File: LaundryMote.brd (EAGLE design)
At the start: 52.5 x 23.3 mm, 6 parts

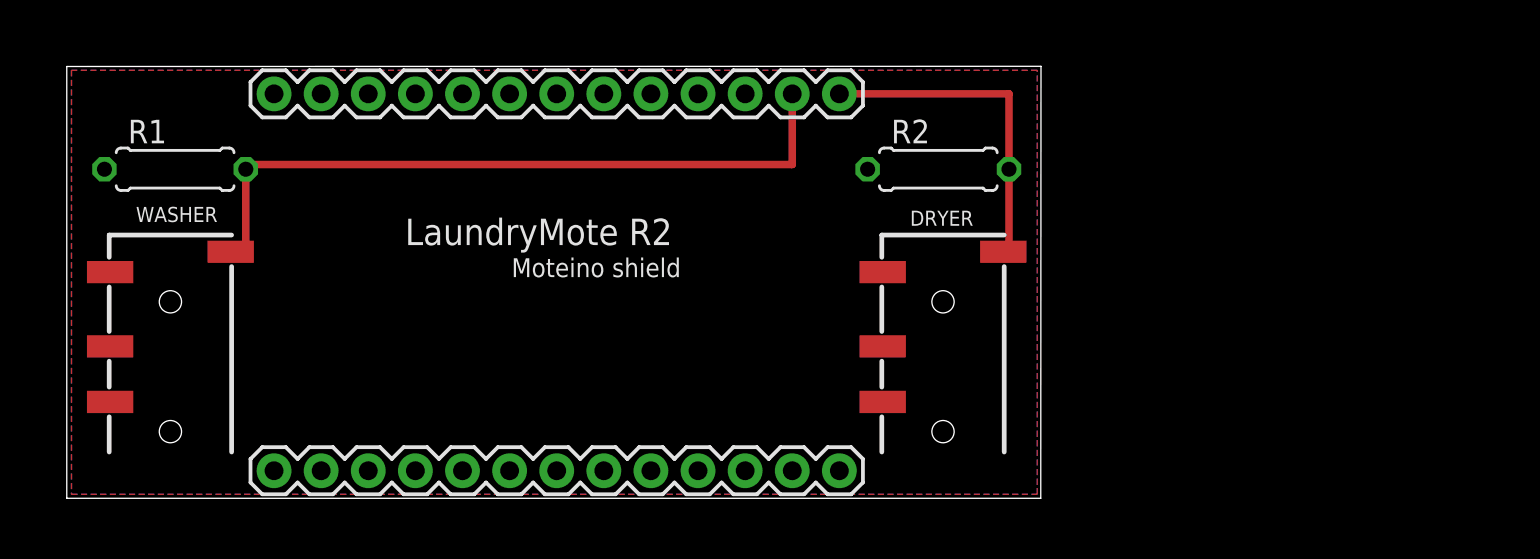
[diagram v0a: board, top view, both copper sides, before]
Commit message: LaundryMote R3 started, NodeJS baseline utility
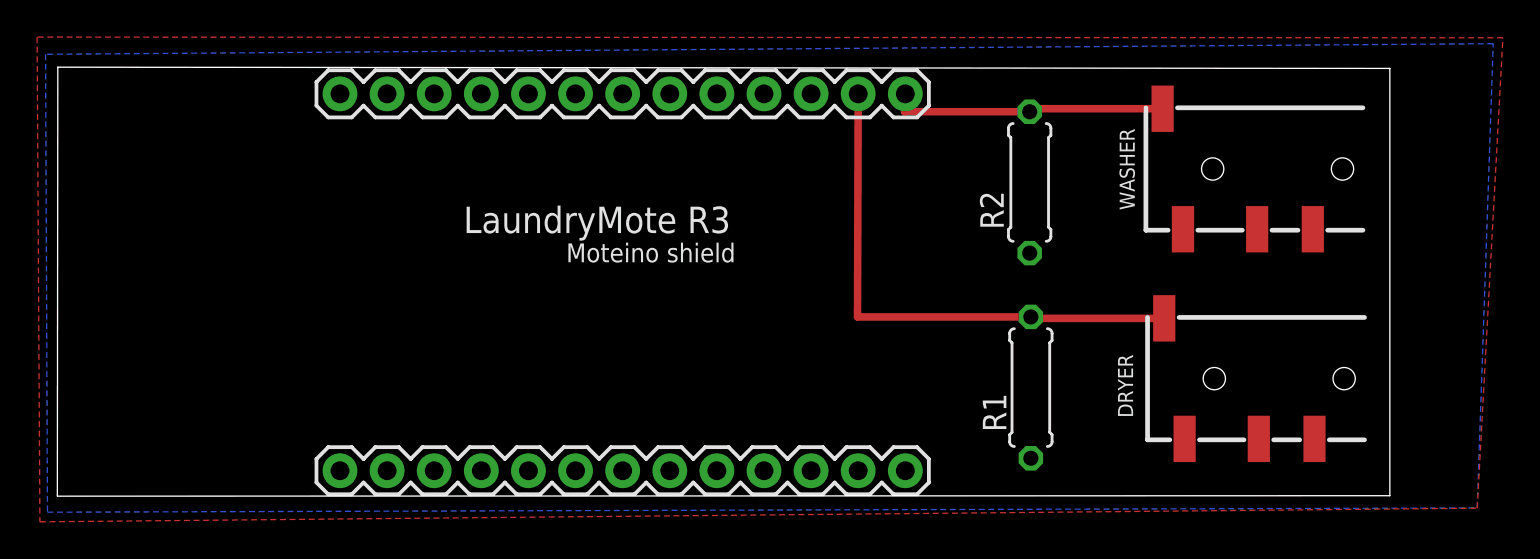
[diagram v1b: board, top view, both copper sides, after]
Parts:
- added E$1: (no value), adafruit:OSHWLOGO_TOL_0.2
- moved WASHER 65.0 mm to (71.5, 7.51), turned to 180 degrees
- moved R1 47.6 mm to (53.0, 7.02), turned to 90 degrees
- moved DRYER 28.0 mm to (71.4, 18.8), turned to 180 degrees
- moved R2 4.98 mm to (52.9, 18.1), turned to 90 degrees
- moved ANALOGSIDE 3.56 mm to (15.7, 22.9)
- moved DIGITALSIDE 3.56 mm to (15.7, 2.54)
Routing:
- net A1: track 38.6 -> 28.6 mm
- net A0: track 18.0 -> 15.0 mm
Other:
- board size 52.5 x 23.3 mm -> 71.8 x 23.1 mm
- board text added: "LaundryMote R3"
- board text removed: "LaundryMote R2"
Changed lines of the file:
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@@
 <board>
 <plain>
-<wire x1="1.016" y1="1.0541" x2="53.5307" y2="1.0541" width="0" layer="20"/>
-<wire x1="53.5307" y1="1.0541" x2="53.5434" y2="24.3459" width="0" layer="20"/>
-<wire x1="53.5434" y1="24.3459" x2="1.016" y2="24.3359" width="0" layer="20"/>
-<wire x1="1.016" y1="24.3359" x2="1.016" y2="1.0541" width="0" layer="20"/>
-<text x="9.144" y="16.764" size="0.8128" layer="25" rot="R180">WASHER</text>
-<text x="46.482" y="15.748" size="0.8128" layer="25">DRYER</text>
-<text x="19.2532" y="14.7066" size="1.4224" layer="25">LaundryMote R2</text>
-<text x="41.91" y="20.32" size="0.8128" layer="27">A0</text>
-<text x="39.37" y="20.32" size="0.8128" layer="27">A1</text>
-<text x="24.9936" y="12.9794" size="1.016" layer="25">Moteino shield</text>
+<wire x1="0.508" y1="1.1684" x2="72.3521" y2="1.1938" width="0" layer="20"/>
+<wire x1="72.3521" y1="1.1938" x2="72.3521" y2="24.2316" width="0" layer="20"/>
+<wire x1="72.3521" y1="24.2316" x2="0.5334" y2="24.2978" width="0" layer="20"/>
+<wire x1="0.5334" y1="24.2978" x2="0.508" y2="1.1684" width="0" layer="20"/>
+<text x="57.785" y="20.9931" size="0.8128" layer="25" rot="R270">WASHER</text>
+<text x="58.5089" y="5.3975" size="0.8128" layer="25" rot="R90">DRYER</text>
+<text x="22.4028" y="15.3543" size="1.4224" layer="25">LaundryMote R3</text>
+<text x="45.339" y="19.6215" size="1.27" layer="27">A0</text>
+<text x="42.7736" y="19.6977" size="1.27" layer="27">A1</text>
+<text x="27.94" y="13.7795" size="1.016" layer="25">Moteino shield</text>
+<rectangle x1="51.7017" y1="2.0574" x2="54.3433" y2="4.2926" layer="41"/>
+<rectangle x1="51.5874" y1="13.0429" x2="54.1147" y2="15.5702" layer="41"/>
 </plain>
 <attributes>
@@
 </autorouter>
 <elements>
-<element name="ANALOGSIDE" library="SparkFun-Connectors" package="1X13" value="M13" x="12.192" y="22.86" smashed="yes">
-<attribute name="OC_NEWARK" value="unknown" x="57.912" y="-1.27" size="1.778" layer="27" display="off"/>
-<attribute name="MPN" value="" x="57.912" y="-1.27" size="1.778" layer="27" display="off"/>
-<attribute name="MF" value="" x="57.912" y="-1.27" size="1.778" layer="27" display="off"/>
-</element>
-<element name="DIGITALSIDE" library="SparkFun-Connectors" package="1X13" value="M13" x="12.192" y="2.54" smashed="yes">
-<attribute name="OC_NEWARK" value="unknown" x="57.912" y="-29.21" size="1.778" layer="27" display="off"/>
-<attribute name="MPN" value="" x="57.912" y="-29.21" size="1.778" layer="27" display="off"/>
-<attribute name="MF" value="" x="57.912" y="-29.21" size="1.778" layer="27" display="off"/>
-</element>
-<element name="WASHER" library="SparkFun-Connectors" package="AUDIO-JACK-TRRS-SMD" value="AUDIO-JACK3" x="6.604" y="3.048" rot="R90">
-<attribute name="OC_NEWARK" value="unknown" x="21.844" y="28.448" size="1.778" layer="27" rot="R90" display="off"/>
-<attribute name="MPN" value="" x="21.844" y="28.448" size="1.778" layer="27" rot="R90" display="off"/>
-<attribute name="MF" value="" x="21.844" y="28.448" size="1.778" layer="27" rot="R90" display="off"/>
-</element>
-<element name="DRYER" library="SparkFun-Connectors" package="AUDIO-JACK-TRRS-SMD" value="AUDIO-JACK3" x="48.26" y="3.048" rot="R90">
-<attribute name="OC_NEWARK" value="unknown" x="53.34" y="28.448" size="1.778" layer="27" rot="R90" display="off"/>
-<attribute name="MPN" value="" x="53.34" y="28.448" size="1.778" layer="27" rot="R90" display="off"/>
-<attribute name="MF" value="" x="53.34" y="28.448" size="1.778" layer="27" rot="R90" display="off"/>
-</element>
-<element name="R1" library="adafruit" package="0207/7" value="" x="6.858" y="18.796"/>
-<element name="R2" library="adafruit" package="0207/7" value="" x="48.006" y="18.796"/>
+<element name="ANALOGSIDE" library="SparkFun-Connectors" package="1X13" value="M13" x="15.748" y="22.86" smashed="yes">
+<attribute name="OC_NEWARK" value="unknown" x="61.468" y="-1.27" size="1.778" layer="27" display="off"/>
+<attribute name="MPN" value="" x="61.468" y="-1.27" size="1.778" layer="27" display="off"/>
+<attribute name="MF" value="" x="61.468" y="-1.27" size="1.778" layer="27" display="off"/>
+</element>
+<element name="DIGITALSIDE" library="SparkFun-Connectors" package="1X13" value="M13" x="15.748" y="2.54" smashed="yes">
+<attribute name="OC_NEWARK" value="unknown" x="61.468" y="-29.21" size="1.778" layer="27" display="off"/>
+<attribute name="MPN" value="" x="61.468" y="-29.21" size="1.778" layer="27" display="off"/>
+<attribute name="MF" value="" x="61.468" y="-29.21" size="1.778" layer="27" display="off"/>
+</element>
+<element name="WASHER" library="SparkFun-Connectors" package="AUDIO-JACK-TRRS-SMD" value="AUDIO-JACK3" x="71.4883" y="7.5057" rot="R180">
+<attribute name="OC_NEWARK" value="unknown" x="46.0883" y="22.7457" size="1.778" layer="27" rot="R180" display="off"/>
+<attribute name="MPN" value="" x="46.0883" y="22.7457" size="1.778" layer="27" rot="R180" display="off"/>
+<attribute name="MF" value="" x="46.0883" y="22.7457" size="1.778" layer="27" rot="R180" display="off"/>
+</element>
+<element name="DRYER" library="SparkFun-Connectors" package="AUDIO-JACK-TRRS-SMD" value="AUDIO-JACK3" x="71.3994" y="18.8087" rot="R180">
+<attribute name="OC_NEWARK" value="unknown" x="45.9994" y="23.8887" size="1.778" layer="27" rot="R180" display="off"/>
+<attribute name="MPN" value="" x="45.9994" y="23.8887" size="1.778" layer="27" rot="R180" display="off"/>
+<attribute name="MF" value="" x="45.9994" y="23.8887" size="1.778" layer="27" rot="R180" display="off"/>
+</element>
+<element name="R1" library="adafruit" package="0207/7" value="" x="52.9971" y="7.0231" smashed="yes" rot="R90">
+<attribute name="NAME" x="51.6763" y="4.6355" size="1.27" layer="25" ratio="10" rot="R90"/>
+<attribute name="VALUE" x="53.5559" y="4.7371" size="1.27" layer="27" ratio="10" rot="R90"/>
+</element>
+<element name="R2" library="adafruit" package="0207/7" value="" x="52.9336" y="18.0848" smashed="yes" rot="R90">
+<attribute name="NAME" x="51.5366" y="15.5448" size="1.27" layer="25" ratio="10" rot="R90"/>
+<attribute name="VALUE" x="53.4924" y="15.7988" size="1.27" layer="27" ratio="10" rot="R90"/>
+</element>
+<element name="E$1" library="adafruit" package="OSHWLOGO_TOL_0.2" value="" x="24.765" y="12.0396"/>
 </elements>
 <signals>
@@
 <contactref element="ANALOGSIDE" pad="1"/>
 <polygon width="0.254" layer="1" isolate="0.4064">
-<vertex x="1.27" y="24.13"/>
-<vertex x="1.27" y="1.27"/>
-<vertex x="53.34" y="1.27"/>
-<vertex x="53.34" y="24.13"/>
-</polygon>
-<polygon width="0.254" layer="16" isolate="0.4064">
-<vertex x="1.27" y="24.13"/>
-<vertex x="1.27" y="1.27"/>
-<vertex x="53.34" y="1.27"/>
-<vertex x="53.34" y="24.13"/>
+<vertex x="-0.5842" y="25.9207"/>
+<vertex x="-0.4318" y="-0.2159"/>
+<vertex x="77.0636" y="0.5207"/>
+<vertex x="78.4479" y="25.8826"/>
 </polygon>
 <contactref element="WASHER" pad="TIP"/>
@@
 <contactref element="DRYER" pad="TIP"/>
 <contactref element="R2" pad="1"/>
+<polygon width="0.254" layer="16" isolate="0.4064">
+<vertex x="-0.127" y="24.9936"/>
+<vertex x="-0.0254" y="0.3048"/>
+<vertex x="77.0636" y="0.5334"/>
+<vertex x="77.9272" y="25.5651"/>
+</polygon>
 </signal>
 <signal name="A1">
@@
 <contactref element="WASHER" pad="EARTH"/>
 <contactref element="R1" pad="2"/>
-<wire x1="9.854" y1="14.348" x2="10.668" y2="14.348" width="0.4064" layer="1"/>
-<wire x1="10.668" y1="18.796" x2="10.922" y2="19.05" width="0.4064" layer="1"/>
-<wire x1="10.922" y1="19.05" x2="40.132" y2="19.05" width="0.4064" layer="1"/>
-<wire x1="40.132" y1="19.05" x2="40.132" y2="22.86" width="0.4064" layer="1"/>
-<wire x1="10.668" y1="14.348" x2="10.668" y2="18.796" width="0.4064" layer="1"/>
+<wire x1="60.1883" y1="10.7557" x2="52.9971" y2="10.7557" width="0.4064" layer="1"/>
+<wire x1="52.9971" y1="10.7557" x2="52.9971" y2="10.8331" width="0.4064" layer="1"/>
+<wire x1="52.9971" y1="10.8331" x2="43.6499" y2="10.8331" width="0.4064" layer="1"/>
+<wire x1="43.6499" y1="10.8331" x2="43.688" y2="22.86" width="0.4064" layer="1"/>
 </signal>
 <signal name="A0">
@@
 <contactref element="DRYER" pad="EARTH"/>
 <contactref element="R2" pad="2"/>
-<wire x1="51.51" y1="14.348" x2="51.816" y2="14.348" width="0.4064" layer="1"/>
-<wire x1="51.816" y1="14.348" x2="51.816" y2="18.796" width="0.4064" layer="1"/>
-<wire x1="51.816" y1="18.796" x2="51.816" y2="22.86" width="0.4064" layer="1"/>
-<wire x1="51.816" y1="22.86" x2="42.672" y2="22.86" width="0.4064" layer="1"/>
+<wire x1="60.0994" y1="22.0587" x2="52.9336" y2="22.0587" width="0.4064" layer="1"/>
+<wire x1="52.9336" y1="22.0587" x2="52.9336" y2="21.8948" width="0.4064" layer="1"/>
+<wire x1="52.9336" y1="21.8948" x2="46.1899" y2="21.8948" width="0.4064" layer="1"/>
+<wire x1="46.1899" y1="21.8948" x2="46.228" y2="22.86" width="0.4064" layer="1"/>
 </signal>
 </signals>
